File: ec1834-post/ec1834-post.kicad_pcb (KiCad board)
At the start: 2 copper layers, 116.9 x 103.7 mm, 28 parts, among them J0 BUS_EC1834_8Bit, J1 Bus_ISA_8bit, J2 Conn_02x07_Odd_Even, J3 Conn_01x03, J4 Conn_02x06_Odd_Even, SW1 SW_DIP_x10, U1 74LS688, U2 74LS86, U3 7432, U4 74HC374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

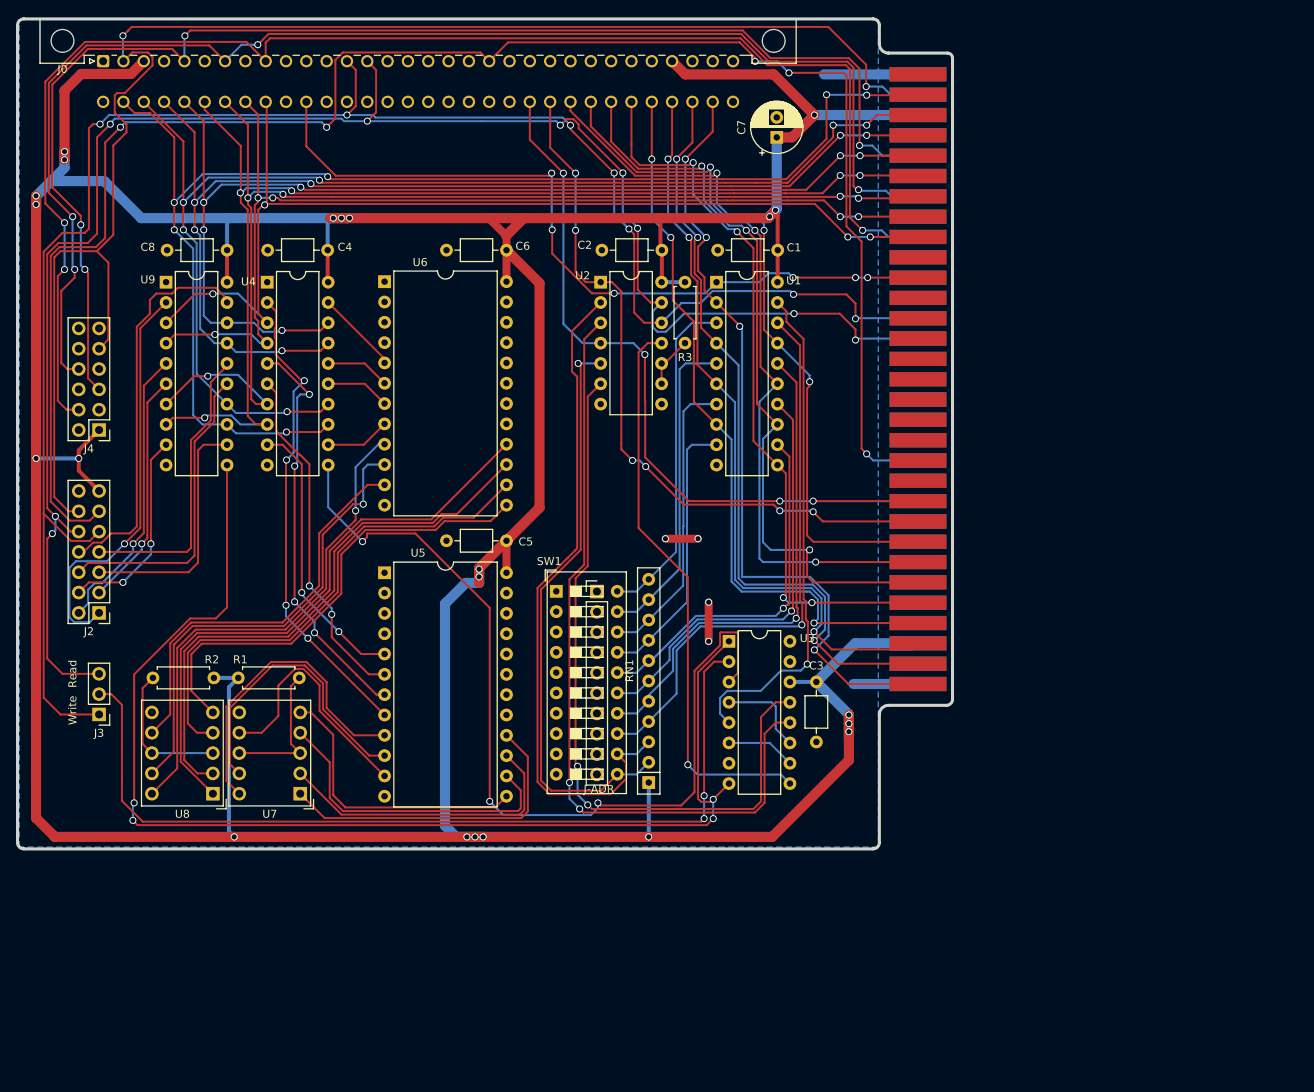
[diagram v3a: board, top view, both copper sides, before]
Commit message: Updated schema, fixed wrong footprint
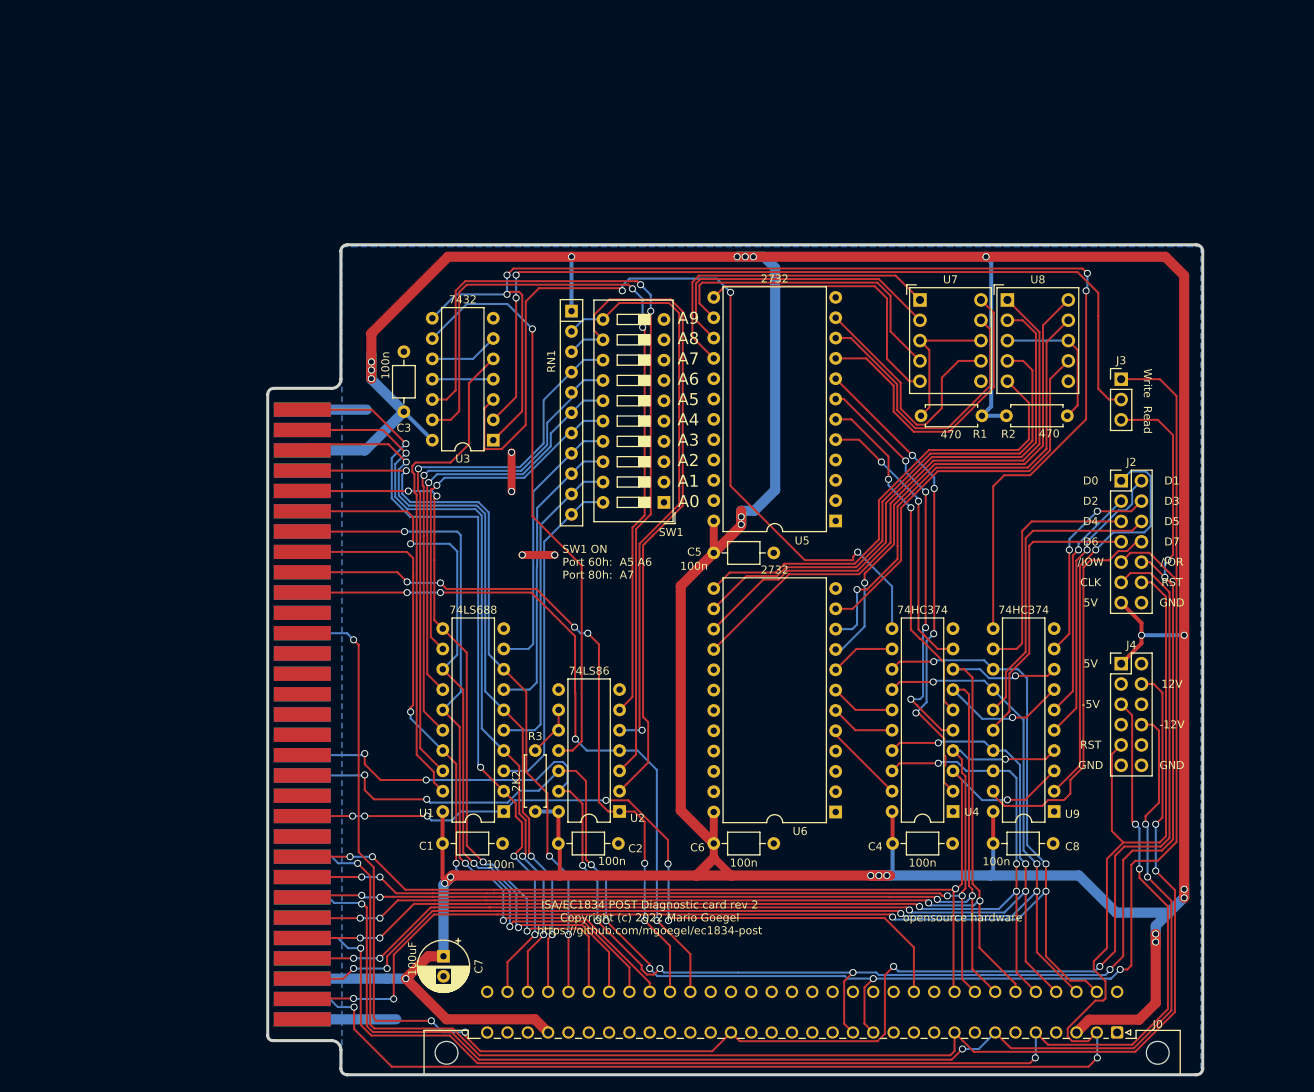
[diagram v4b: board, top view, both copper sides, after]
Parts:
- removed J-ADR: IO-ADDR, Connector_PinHeader_2.54mm:PinHeader_1x10_P2.54mm_Vertical
- U3: footprint Package_DIP:DIP-16_W7.62mm -> Package_DIP:DIP-14_W7.62mm
- moved J0 175.5 mm to (156.5, 147.7), turned to 180 degrees
- moved J3 134.5 mm to (157.0, 66.0), turned to 0 degrees
- moved J4 131.1 mm to (157.0, 101.6), turned to 0 degrees
- moved U9 129.2 mm to (148.6, 120.1), turned to 180 degrees
- moved J2 128.8 mm to (157.0, 78.7), turned to 0 degrees
- moved C8 121.1 mm to (141.0, 124.1), turned to 0 degrees
- moved R2 118.9 mm to (150.2, 70.6), turned to 180 degrees
- moved U8 116.9 mm to (142.7, 56.1), turned to 0 degrees
- moved C7 110.5 mm to (72.3, 138.2), turned to 270 degrees
- moved U4 108.3 mm to (136.0, 120.1), turned to 180 degrees
- moved C4 102.4 mm to (128.4, 124.1), turned to 0 degrees
- moved U7 99.1 mm to (131.8, 56.1), turned to 0 degrees
- moved J1 88.1 mm to (54.4, 108.0), turned to 270 degrees
- moved U6 87.0 mm to (121.3, 120.1), turned to 180 degrees
- moved C1 85.2 mm to (72.1, 124.1), turned to 0 degrees
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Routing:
- net Net-(U3-Pad1): track 153.1 -> 159.1 mm
- net /SELA9: track 91.8 -> 95.5 mm
- net Net-(U3-Pad11): track 11.4 -> 7.62 mm
- net /SELA8: track 99.1 -> 102.5 mm
- net IOWIOR: track 111.4 -> 108.7 mm
- net ENLATCH: track 71.2 -> 73.1 mm
- net +5V: track 576.6 -> 578.3 mm
- net Net-(U3-Pad3): track 114.2 -> 112.6 mm
- net /SEL_AD: track 63.0 -> 62.4 mm, vias 1 -> 0
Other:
- outline, holes or cut-outs redrawn
- board text added: "-12V"
- board text added: "-5V"
- board text added: "/IOR"
- board text added: "/IOW"
- board text added: "12V"
- board text added: "5V"
- board text added: "A0"
- board text added: "A1"
- board text added: "A2"
- board text added: "A3"
- board text added: "A4"
- board text added: "A5"
- board text added: "A6"
- board text added: "A7"
- board text added: "A8"
- board text added: "A9"
- board text added: "CLK"
- board text added: "D0"
- board text added: "D1"
- board text added: "D2"
- board text added: "D3"
- board text added: "D4"
- board text added: "D5"
- board text added: "D6"
- board text added: "D7"
- board text added: "GND"
- board text added: "ISA/EC1834 POST Diagnostic card rev 2 Copyright (c) 2022 Mario Goegel https://github.com/mgoegel/ec1834-post"
- board text added: "RST"
- board text added: "SW1 ON Port 60h: A5 A6 Port 80h: A7"
- board text added: "opensource hardware"
